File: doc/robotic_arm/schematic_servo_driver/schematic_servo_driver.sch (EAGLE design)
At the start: 1 part

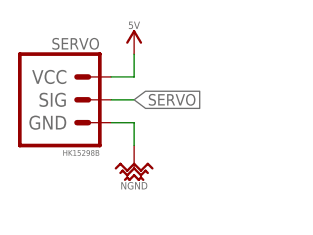
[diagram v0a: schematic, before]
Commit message: Create mcu to unity example code.  Create schematics for master thesis.  Edit robotic arm and touch glove pcb.
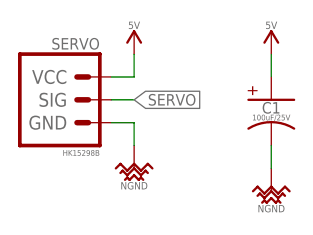
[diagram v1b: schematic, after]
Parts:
- added C1: 100uF/25V, _capacitors:100UF-POLARIZED_SMD_25V-20%_DIA5-LS2-H11
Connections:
- net 5V: now also C1.A
- net NGND: now also C1.K
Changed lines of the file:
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@@
 <setting verticaltext="up"/>
 </settings>
-<grid distance="0.1" unitdist="inch" unit="inch" style="lines" multiple="1" display="no" altdistance="0.01" altunitdist="inch" altunit="inch"/>
+<grid distance="0.1" unitdist="inch" unit="inch" style="lines" multiple="1" display="yes" altdistance="0.01" altunitdist="inch" altunit="inch"/>
 <layers>
 <layer number="1" name="Top" color="4" fill="1" visible="no" active="no"/>
@@
 <part name="SUPPLY1" library="_power_symbols" deviceset="NGND" device=""/>
 <part name="SUPPLY2" library="_power_symbols" deviceset="5V" device=""/>
+<part name="C1" library="_capacitors" deviceset="100UF-POLARIZED" device="_SMD_25V-20%_DIA5-LS2-H11" package3d_urn="urn:adsk.eagle:package:5948134/2" value="100uF/25V"/>
+<part name="SUPPLY3" library="_power_symbols" deviceset="5V" device=""/>
+<part name="SUPPLY4" library="_power_symbols" deviceset="NGND" device=""/>
 </parts>
 <sheets>
@@
 <instance part="SUPPLY1" gate="G$1" x="35.56" y="17.78" smashed="yes"/>
 <instance part="SUPPLY2" gate="5V" x="35.56" y="30.48" smashed="yes"/>
+<instance part="C1" gate="G$1" x="50.8" y="25.4" smashed="yes">
+<attribute name="NAME" x="50.8" y="25.146" size="1.27" layer="95" font="vector" ratio="10" align="top-center"/>
+<attribute name="VALUE" x="50.8" y="23.114" size="0.635" layer="96" font="vector" ratio="10" align="bottom-center"/>
+</instance>
+<instance part="SUPPLY3" gate="5V" x="50.8" y="30.48" smashed="yes"/>
+<instance part="SUPPLY4" gate="G$1" x="50.8" y="15.24" smashed="yes"/>
 </instances>
 <busses>
@@
 <wire x1="35.56" y1="27.94" x2="35.56" y2="30.48" width="0.1524" layer="91"/>
 </segment>
+<segment>
+<pinref part="C1" gate="G$1" pin="A"/>
+<pinref part="SUPPLY3" gate="5V" pin="5V"/>
+<wire x1="50.8" y1="27.94" x2="50.8" y2="30.48" width="0.1524" layer="91"/>
+</segment>
 </net>
 <net name="NGND" class="0">
@@
 <wire x1="35.56" y1="22.86" x2="35.56" y2="20.32" width="0.1524" layer="91"/>
 </segment>
+<segment>
+<pinref part="SUPPLY4" gate="G$1" pin="NGND"/>
+<pinref part="C1" gate="G$1" pin="K"/>
+<wire x1="50.8" y1="17.78" x2="50.8" y2="20.32" width="0.1524" layer="91"/>
+</segment>
 </net>
